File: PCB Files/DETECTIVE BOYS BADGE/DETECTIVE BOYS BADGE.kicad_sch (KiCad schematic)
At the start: 38 parts, among them J1 Jack 3.5mm, SW1 SPDT_PCM12, SW2 Pushbutton, U1 NRF24L01_Breakout, U2 MIC5205-3.3YM5, U3 TP4056, U4 LM358, U5 ATmega328P-A, X1 Resonator 8MHz

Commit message: Updated PCB version to v1.1
Fixed some schematic error designs at audio amplifier circuit, modified NRF24 mini footprint to easier placement.
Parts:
- C7, C9: value 100nF -> 330nF
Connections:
- net BAT: no longer SW1.1 (A)
- net VBUS: no longer SW1.3 (C)
- new net VBAT: SW1.1 (A)
- no-connect marks 24 -> 25
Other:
- note added: "Detective Boys walkie talkie v1.1 (28/06/2022)"
- note added: "Mandatory low pass filter. Using R=330 and C=330n sets cutoff frequency at 1.4kHz Filters pwm high frequency and allows human voice frequencies"
- note removed: "Mandatory low pass filter. Using R=330 and C=100n sets cutoff frequency at 4.8kHz Filters pwm high frequency and allows human voice frequencies"

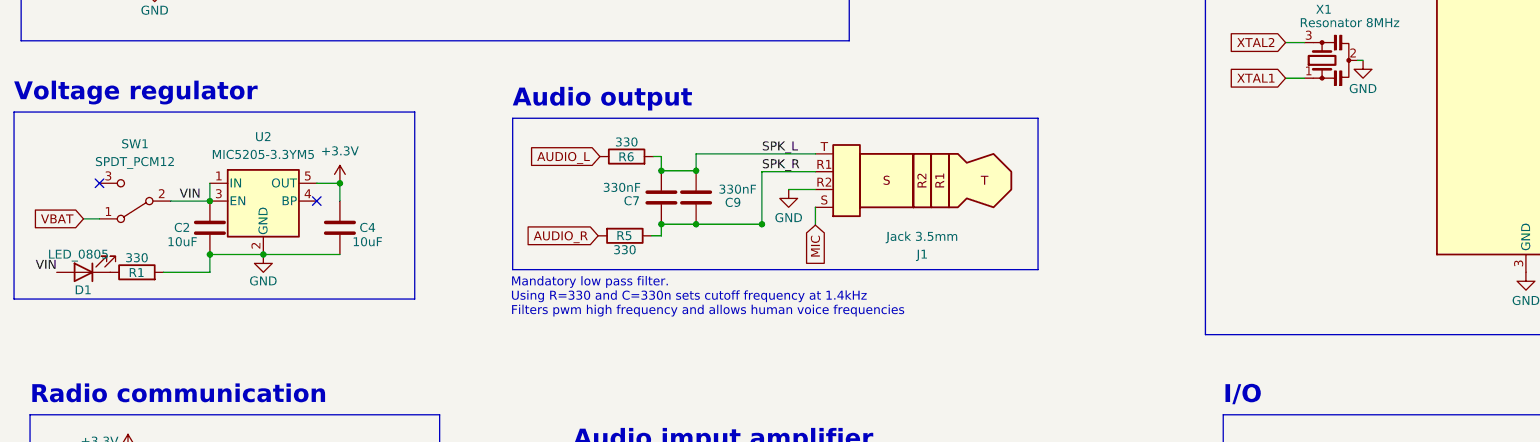
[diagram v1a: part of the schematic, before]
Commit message: Updated PCB (v1.2)
Added a flexPCB connector on the edge of the board connected to the ICSP pins, making easier to program the ATMEGA328P.
The battery terminals footprint is now only on one side of the board, preventing accidental short-circuit on the bottom side.
Moved some components to allow more space for the LiPo battery.
Changed the values of components C7,C9 R5,R6, adjusting the values for filtering the audio output.
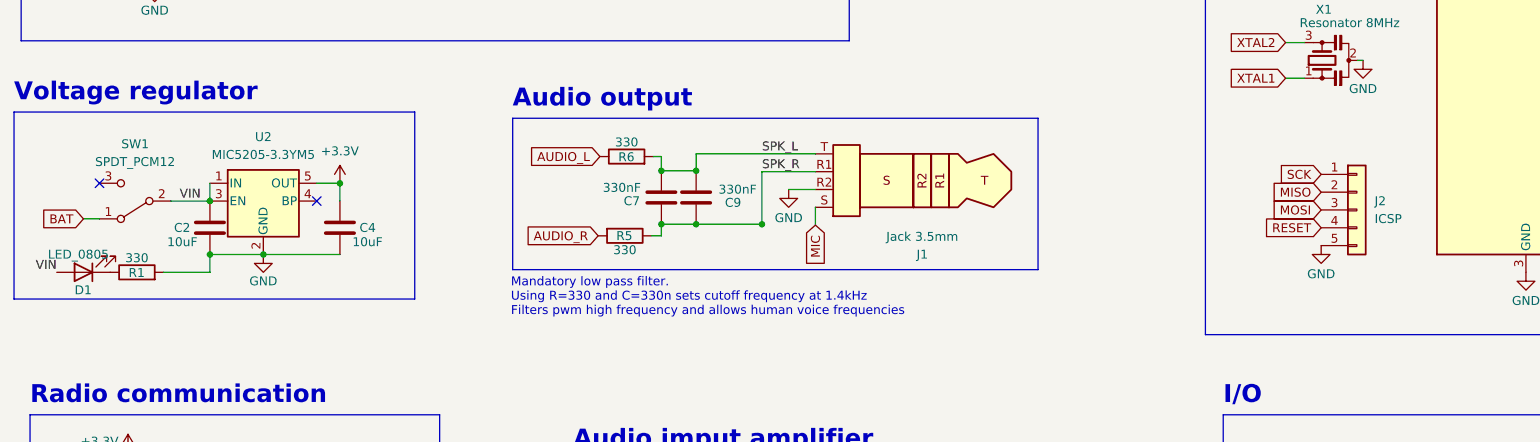
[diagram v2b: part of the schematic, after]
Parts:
- added J2: ICSP, Connector_FFC-FPC:Molex_200528-0050_1x05-1MP_P1.00mm_Horizontal, symbol Connector_Generic:Conn_01x05
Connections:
- net VBAT is gone; now on net BAT: SW1.1 (A)
- net GND: now also J2.5 (Pin_5)
- net MISO: now also J2.2 (Pin_2)
- net MOSI: now also J2.3 (Pin_3)
- net RESET: now also J2.4 (Pin_4)
- net SCK: now also J2.1 (Pin_1)
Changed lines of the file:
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@@
+    )
+  )
+  (global_label "MISO" (shape input) (at 209.55 100.33 180) (fields_autoplaced)
+    (effects (font (size 1.27 1.27)) (justify right))
+    (property "Intersheet References" "${INTERSHEET_REFS}" (id 0) (at 202.5407 100.2506 0)
+      (effects (font (size 1.27 1.27)) (justify right) hide)
     )
   )
@@
     )
   )
+  (global_label "SCK" (shape input) (at 209.55 97.79 180) (fields_autoplaced)
+    (effects (font (size 1.27 1.27)) (justify right))
+    (property "Intersheet References" "${INTERSHEET_REFS}" (id 0) (at 203.3874 97.7106 0)
+      (effects (font (size 1.27 1.27)) (justify right) hide)
+    )
+  )
   (global_label "XTAL1" (shape input) (at 254 58.42 0) (fields_autoplaced)
     (effects (font (size 1.27 1.27)) (justify left))
@@
     )
   )
+  (global_label "MOSI" (shape input) (at 209.55 102.87 180) (fields_autoplaced)
+    (effects (font (size 1.27 1.27)) (justify right))
+    (property "Intersheet References" "${INTERSHEET_REFS}" (id 0) (at 202.5407 102.7906 0)
+      (effects (font (size 1.27 1.27)) (justify right) hide)
+    )
+  )
   (global_label "AUDIO_L" (shape input) (at 254 45.72 0) (fields_autoplaced)
     (effects (font (size 1.27 1.27)) (justify left))
@@
     )
   )
+  (global_label "RESET" (shape input) (at 209.55 105.41 180) (fields_autoplaced)
+    (effects (font (size 1.27 1.27)) (justify right))
+    (property "Intersheet References" "${INTERSHEET_REFS}" (id 0) (at 201.3917 105.4894 0)
+      (effects (font (size 1.27 1.27)) (justify right) hide)
+    )
+  )
   (global_label "SCK" (shape input) (at 39.37 157.48 180) (fields_autoplaced)
     (effects (font (size 1.27 1.27)) (justify right))
@@
     )
   )
-  (global_label "VBAT" (shape input) (at 33.02 104.14 180) (fields_autoplaced)
-    (effects (font (size 1.27 1.27)) (justify right))
-    (property "Intersheet References" "${INTERSHEET_REFS}" (id 0) (at 26.1921 104.0606 0)
+  (global_label "BAT" (shape input) (at 33.02 104.14 180) (fields_autoplaced)
+    (effects (font (size 1.27 1.27)) (justify right))
+    (property "Intersheet References" "${INTERSHEET_REFS}" (id 0) (at 27.2807 104.0606 0)
       (effects (font (size 1.27 1.27)) (justify right) hide)
     )
@@
     (pin "8")
   )
+  (symbol (lib_id "power:GND") (at 209.55 107.95 0) (unit 1)
+    (in_bom yes) (on_board yes)
+    (property "Reference" "#PWR030" (id 0) (at 209.55 114.3 0)
+      (effects (font (size 1.27 1.27)) hide)
+    )
+    (property "Value" "GND" (id 1) (at 209.55 112.014 0))
+    (property "Footprint" "" (id 2) (at 209.55 107.95 0)
+      (effects (font (size 1.27 1.27)) hide)
+    )
+    (property "Datasheet" "" (id 3) (at 209.55 107.95 0)
+      (effects (font (size 1.27 1.27)) hide)
+    )
+    (pin "1")
+  )
   (symbol (lib_id "Device:R") (at 129.032 168.656 180) (unit 1)
     (in_bom yes) (on_board yes)
@@
     (pin "1")
   )
+  (symbol (lib_id "Connector_Generic:Conn_01x05") (at 214.63 102.87 0) (unit 1)
+    (in_bom yes) (on_board yes) (fields_autoplaced)
+    (property "Reference" "J2" (id 0) (at 217.17 101.5999 0)
+      (effects (font (size 1.27 1.27)) (justify left))
+    )
+    (property "Value" "ICSP" (id 1) (at 217.17 104.1399 0)
+      (effects (font (size 1.27 1.27)) (justify left))
+    )
+    (property "Footprint" "Connector_FFC-FPC:Molex_200528-0050_1x05-1MP_P1.00mm_Horizontal" (id 2) (at 214.63 102.87 0)
+      (effects (font (size 1.27 1.27)) hide)
+    )
+    (property "Datasheet" "~" (id 3) (at 214.63 102.87 0)
+      (effects (font (size 1.27 1.27)) hide)
+    )
+    (pin "1")
+    (pin "2")
+    (pin "3")
+    (pin "4")
+    (pin "5")
+  )
   (symbol (lib_id "Device:C") (at 115.443 101.092 180) (unit 1)
     (in_bom yes) (on_board yes)
@@
       (reference "#PWR029") (unit 1) (value "GND") (footprint "")
     )
+    (path "/7220e41d-2ab9-4158-a2f5-bf66a879658f"
+      (reference "#PWR030") (unit 1) (value "GND") (footprint "")
+    )
     (path "/19e0c3e6-5d97-4210-9017-cc326de5bb6d"
       (reference "BT1") (unit 1) (value "LiPo 100mAh") (footprint "Connector_PinSocket_2.54mm:PinSocket_1x02_P2.54mm_Vertical")
@@
       (reference "J1") (unit 1) (value "Jack 3.5mm") (footprint "Connector_Audio:Jack_3.5mm_PJ320D_Horizontal")
     )
+    (path "/edfb90ce-23fe-4dab-b3de-5d627590e04b"
+      (reference "J2") (unit 1) (value "ICSP") (footprint "Connector_FFC-FPC:Molex_200528-0050_1x05-1MP_P1.00mm_Horizontal")
+    )
     (path "/7b94665f-8fb3-4589-b625-5ab7c5aef882"

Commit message: Updated Schematic PDF file
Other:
- note added: "Detective Boys walkie talkie v1.2 (21/06/2023)"
- note removed: "Detective Boys walkie talkie v1.1 (28/06/2022)"
- moved on the sheet: J2
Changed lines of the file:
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@@
     (effects (font (size 2.54 2.54) (thickness 0.508) bold) (justify left bottom))
   )
-  (text "Detective Boys walkie talkie\nv1.1\n(28/06/2022)" (at 177.9643 179.9857 0)
+  (text "Detective Boys walkie talkie\nv1.2\n(21/06/2023)" (at 177.9643 179.9857 0)
     (effects (font (size 2.54 2.54) (thickness 0.508) bold) (justify left bottom))
   )
@@
     )
   )
-  (global_label "MISO" (shape input) (at 209.55 100.33 180) (fields_autoplaced)
-    (effects (font (size 1.27 1.27)) (justify right))
-    (property "Intersheet References" "${INTERSHEET_REFS}" (id 0) (at 202.5407 100.2506 0)
+  (global_label "MISO" (shape input) (at 243.84 142.24 180) (fields_autoplaced)
+    (effects (font (size 1.27 1.27)) (justify right))
+    (property "Intersheet References" "${INTERSHEET_REFS}" (id 0) (at 236.8307 142.1606 0)
       (effects (font (size 1.27 1.27)) (justify right) hide)
     )
@@
     )
   )
-  (global_label "SCK" (shape input) (at 209.55 97.79 180) (fields_autoplaced)
-    (effects (font (size 1.27 1.27)) (justify right))
-    (property "Intersheet References" "${INTERSHEET_REFS}" (id 0) (at 203.3874 97.7106 0)
+  (global_label "SCK" (shape input) (at 243.84 139.7 180) (fields_autoplaced)
+    (effects (font (size 1.27 1.27)) (justify right))
+    (property "Intersheet References" "${INTERSHEET_REFS}" (id 0) (at 237.6774 139.6206 0)
       (effects (font (size 1.27 1.27)) (justify right) hide)
     )
@@
     )
   )
-  (global_label "MOSI" (shape input) (at 209.55 102.87 180) (fields_autoplaced)
-    (effects (font (size 1.27 1.27)) (justify right))
-    (property "Intersheet References" "${INTERSHEET_REFS}" (id 0) (at 202.5407 102.7906 0)
+  (global_label "MOSI" (shape input) (at 243.84 144.78 180) (fields_autoplaced)
+    (effects (font (size 1.27 1.27)) (justify right))
+    (property "Intersheet References" "${INTERSHEET_REFS}" (id 0) (at 236.8307 144.7006 0)
       (effects (font (size 1.27 1.27)) (justify right) hide)
     )
@@
     )
   )
-  (global_label "RESET" (shape input) (at 209.55 105.41 180) (fields_autoplaced)
-    (effects (font (size 1.27 1.27)) (justify right))
-    (property "Intersheet References" "${INTERSHEET_REFS}" (id 0) (at 201.3917 105.4894 0)
+  (global_label "RESET" (shape input) (at 243.84 147.32 180) (fields_autoplaced)
+    (effects (font (size 1.27 1.27)) (justify right))
+    (property "Intersheet References" "${INTERSHEET_REFS}" (id 0) (at 235.6817 147.3994 0)
       (effects (font (size 1.27 1.27)) (justify right) hide)
     )
@@
     (pin "8")
   )
-  (symbol (lib_id "power:GND") (at 209.55 107.95 0) (unit 1)
-    (in_bom yes) (on_board yes)
-    (property "Reference" "#PWR030" (id 0) (at 209.55 114.3 0)
-      (effects (font (size 1.27 1.27)) hide)
-    )
-    (property "Value" "GND" (id 1) (at 209.55 112.014 0))
-    (property "Footprint" "" (id 2) (at 209.55 107.95 0)
-      (effects (font (size 1.27 1.27)) hide)
-    )
-    (property "Datasheet" "" (id 3) (at 209.55 107.95 0)
+  (symbol (lib_id "power:GND") (at 243.84 149.86 0) (unit 1)
+    (in_bom yes) (on_board yes)
+    (property "Reference" "#PWR030" (id 0) (at 243.84 156.21 0)
+      (effects (font (size 1.27 1.27)) hide)
+    )
+    (property "Value" "GND" (id 1) (at 243.84 153.924 0))
+    (property "Footprint" "" (id 2) (at 243.84 149.86 0)
+      (effects (font (size 1.27 1.27)) hide)
+    )
+    (property "Datasheet" "" (id 3) (at 243.84 149.86 0)
       (effects (font (size 1.27 1.27)) hide)
     )
@@
     (pin "1")
   )
-  (symbol (lib_id "Connector_Generic:Conn_01x05") (at 214.63 102.87 0) (unit 1)
-    (in_bom yes) (on_board yes) (fields_autoplaced)
-    (property "Reference" "J2" (id 0) (at 217.17 101.5999 0)
-      (effects (font (size 1.27 1.27)) (justify left))
-    )
-    (property "Value" "ICSP" (id 1) (at 217.17 104.1399 0)
-      (effects (font (size 1.27 1.27)) (justify left))
-    )
-    (property "Footprint" "Connector_FFC-FPC:Molex_200528-0050_1x05-1MP_P1.00mm_Horizontal" (id 2) (at 214.63 102.87 0)
-      (effects (font (size 1.27 1.27)) hide)
-    )
-    (property "Datasheet" "~" (id 3) (at 214.63 102.87 0)
-      (effects (font (size 1.27 1.27)) hide)
-    )
+  (symbol (lib_id "Connector_Generic:Conn_01x05") (at 248.92 144.78 0) (unit 1)
+    (in_bom yes) (on_board yes) (fields_autoplaced)
+    (property "Reference" "J2" (id 0) (at 251.46 143.5099 0)
+      (effects (font (size 1.27 1.27)) (justify left))
+    )
+    (property "Value" "ICSP" (id 1) (at 251.46 146.0499 0)
+      (effects (font (size 1.27 1.27)) (justify left))
+    )
+    (property "Footprint" "Connector_FFC-FPC:Molex_200528-0050_1x05-1MP_P1.00mm_Horizontal" (id 2) (at 248.92 144.78 0)
+      (effects (font (size 1.27 1.27)) hide)
+    )
+    (property "Datasheet" "~" (id 3) (at 248.92 144.78 0)
+      (effects (font (size 1.27 1.27)) hide)
+    )
